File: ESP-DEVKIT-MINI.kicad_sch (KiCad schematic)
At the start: 45 parts, among them J1 Conn_01x22_Pin, J2 Conn_01x22_Pin, J3 USB_C_Receptacle_USB2.0, J4 USB_B_Mini, J5 USB_B_Micro, Q1 L8050QLT1G, Q2 L8050QLT1G, SW1 SW_Omron_B3FS, SW2 SW_Omron_B3FS, U1 ESP32-S3-MINI-1-N8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

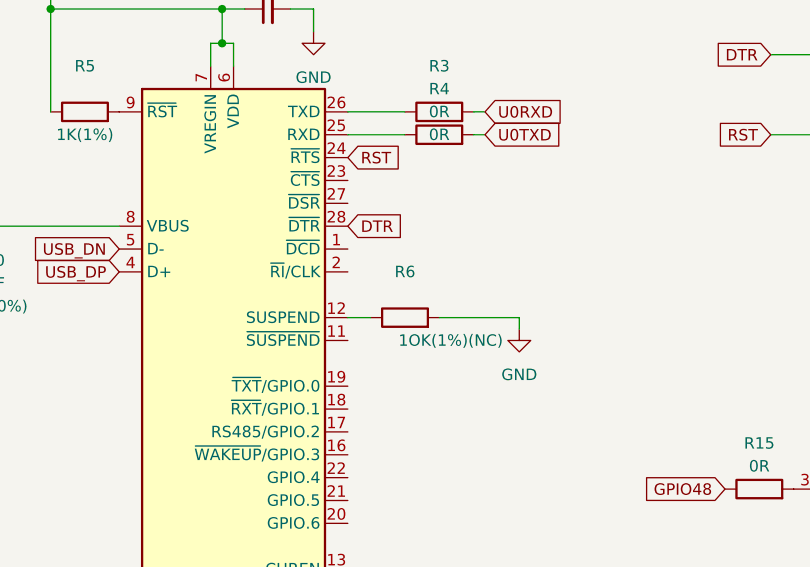
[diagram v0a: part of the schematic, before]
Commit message: Reorganizing the Silk screen
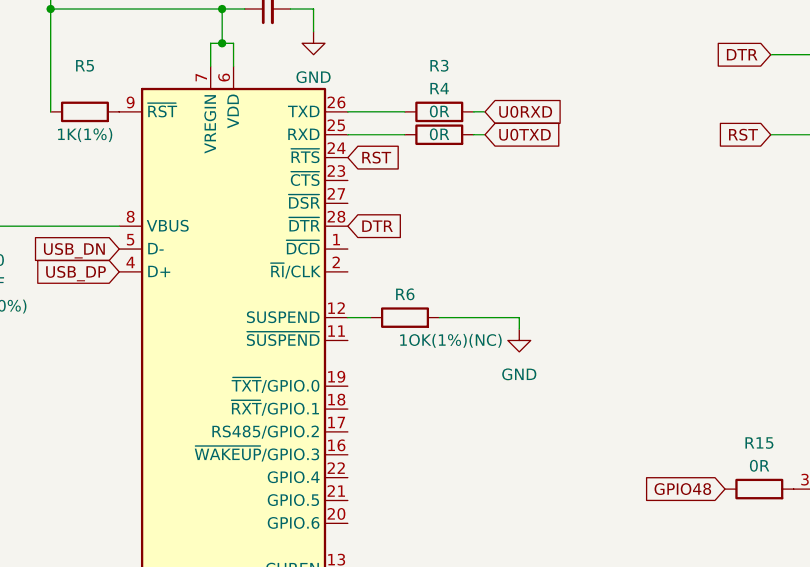
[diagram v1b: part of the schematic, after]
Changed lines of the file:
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@@
   (symbol (lib_id "PCM_4ms_Resistor:0R_0603") (at 86.36 146.05 90) (unit 1)
     (in_bom yes) (on_board yes) (dnp no)
-    (property "Reference" "R6" (at 86.36 140.97 90)
+    (property "Reference" "R6" (at 86.36 143.51 90)
       (effects (font (size 1.27 1.27)))
     )
